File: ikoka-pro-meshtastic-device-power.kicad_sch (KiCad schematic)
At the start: 29 parts, among them J1 Barrel_Jack_Switch, J4 Conn_01x01, J5 Conn_01x01, J6 Conn_01x01, J7 Conn_01x01, U1 BQ24074RGT, U2 MT3608B

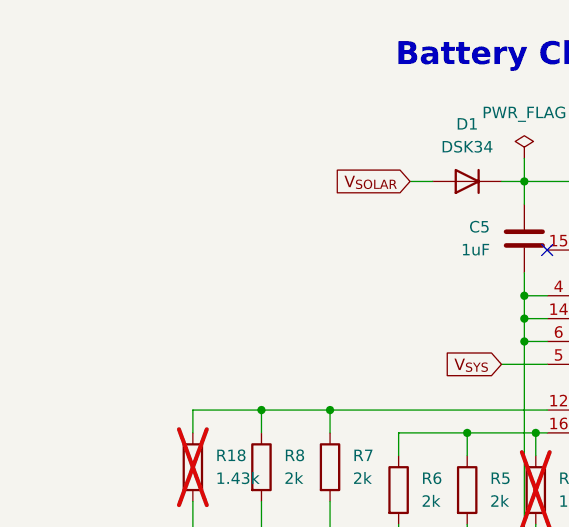
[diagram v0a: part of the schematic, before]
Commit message: feat: I2C and 100k+300k VBAT divider
Fixes #1

Signed-off-by: Andrew Yong <me@ndoo.sg>
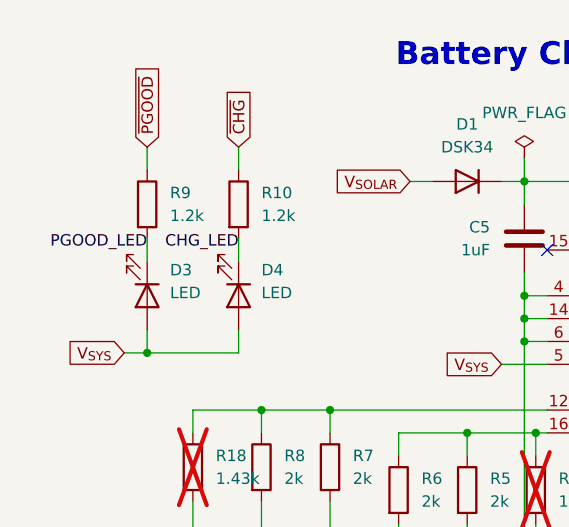
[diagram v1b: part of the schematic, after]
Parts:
- added D3, D4: LED, LED_SMD:LED_0603_1608Metric, symbol Device:LED
- added R10, R9: 1.2k, Resistor_SMD:R_0402_1005Metric, symbol Device:R
- C1, C2: LCSC C59461 -> C23733
- C3: LCSC (none) -> C59461
- C5: LCSC C59461 -> C52923
- C6, C7: LCSC C59461 -> C16780
- D8: LCSC C42371545 -> C19077604
- F1: LCSC (none) -> C42369221
- R1: LCSC C22790 -> C25774
- R18, R19: LCSC (none) -> C25867
- R2: LCSC C22843 -> C25783
- R3: LCSC (none) -> C25774
- R4: LCSC (none) -> C25744
- R5, R6, R7, R8: LCSC (none) -> C4109
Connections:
- net V_{SYS}: now also D3.2 (A), D4.2 (A)
- net ~{CHG}: now also R10.1
- net ~{PGOOD}: now also R9.1
- new net CHG_LED: D4.1 (K), R10.2
- new net PGOOD_LED: D3.1 (K), R9.2

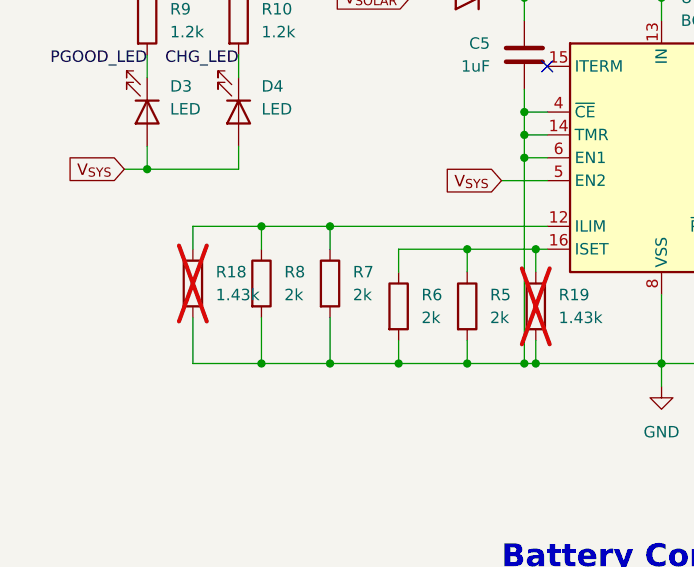
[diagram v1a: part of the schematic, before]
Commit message: fix: Use correct resistor values for ILIM and default to 1.5A (fixes #7)
Signed-off-by: Andrew Yong <me@ndoo.sg>
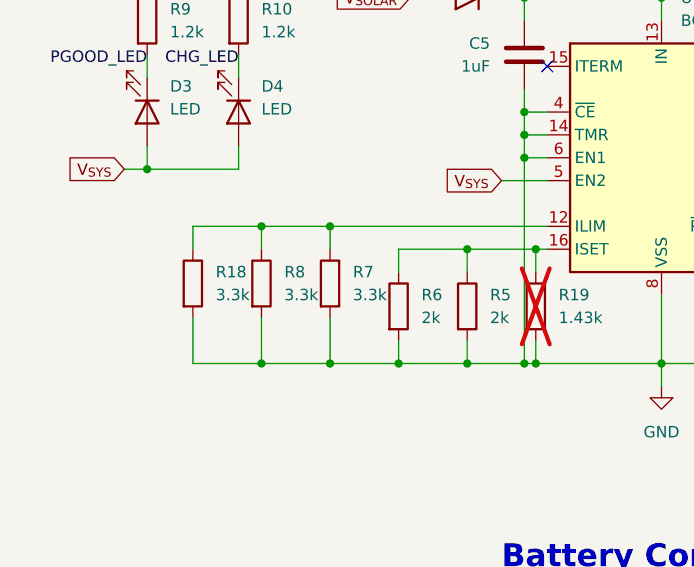
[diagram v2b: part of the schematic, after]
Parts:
- R18: value 1.43k -> 3.3k; LCSC C25867 -> C25890; now fitted
- R7, R8: value 2k -> 3.3k; LCSC C4109 -> C25890
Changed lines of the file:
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@@
 			)
 		)
-		(property "Value" "2k"
+		(property "Value" "3.3k"
 			(at 45.72 97.7899 0)
 			(effects
@@
 			)
 		)
-		(property "LCSC" "C4109"
+		(property "LCSC" "C25890"
 			(at 45.72 95.2499 0)
 			(effects
@@
 			)
 		)
-		(property "Value" "2k"
+		(property "Value" "3.3k"
 			(at 53.34 97.7899 0)
 			(effects
@@
 			)
 		)
-		(property "LCSC" "C4109"
+		(property "LCSC" "C25890"
 			(at 53.34 95.2499 0)
 			(effects
@@
 		(in_bom no)
 		(on_board yes)
-		(dnp yes)
+		(dnp no)
 		(property "Reference" "R18"
 			(at 38.1 95.2499 0)
@@
 			)
 		)
-		(property "Value" "1.43k"
+		(property "Value" "3.3k"
 			(at 38.1 97.7899 0)
 			(effects
@@
 			)
 		)
-		(property "LCSC" "C25867"
+		(property "LCSC" "C25890"
 			(at 38.1 95.2499 0)
 			(effects
